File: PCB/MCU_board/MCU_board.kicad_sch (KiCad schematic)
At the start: 4 parts, among them IC3 ESP32-S3-WROOM-1-N4R8, J13 Conn_01x15, J14 Conn_01x15

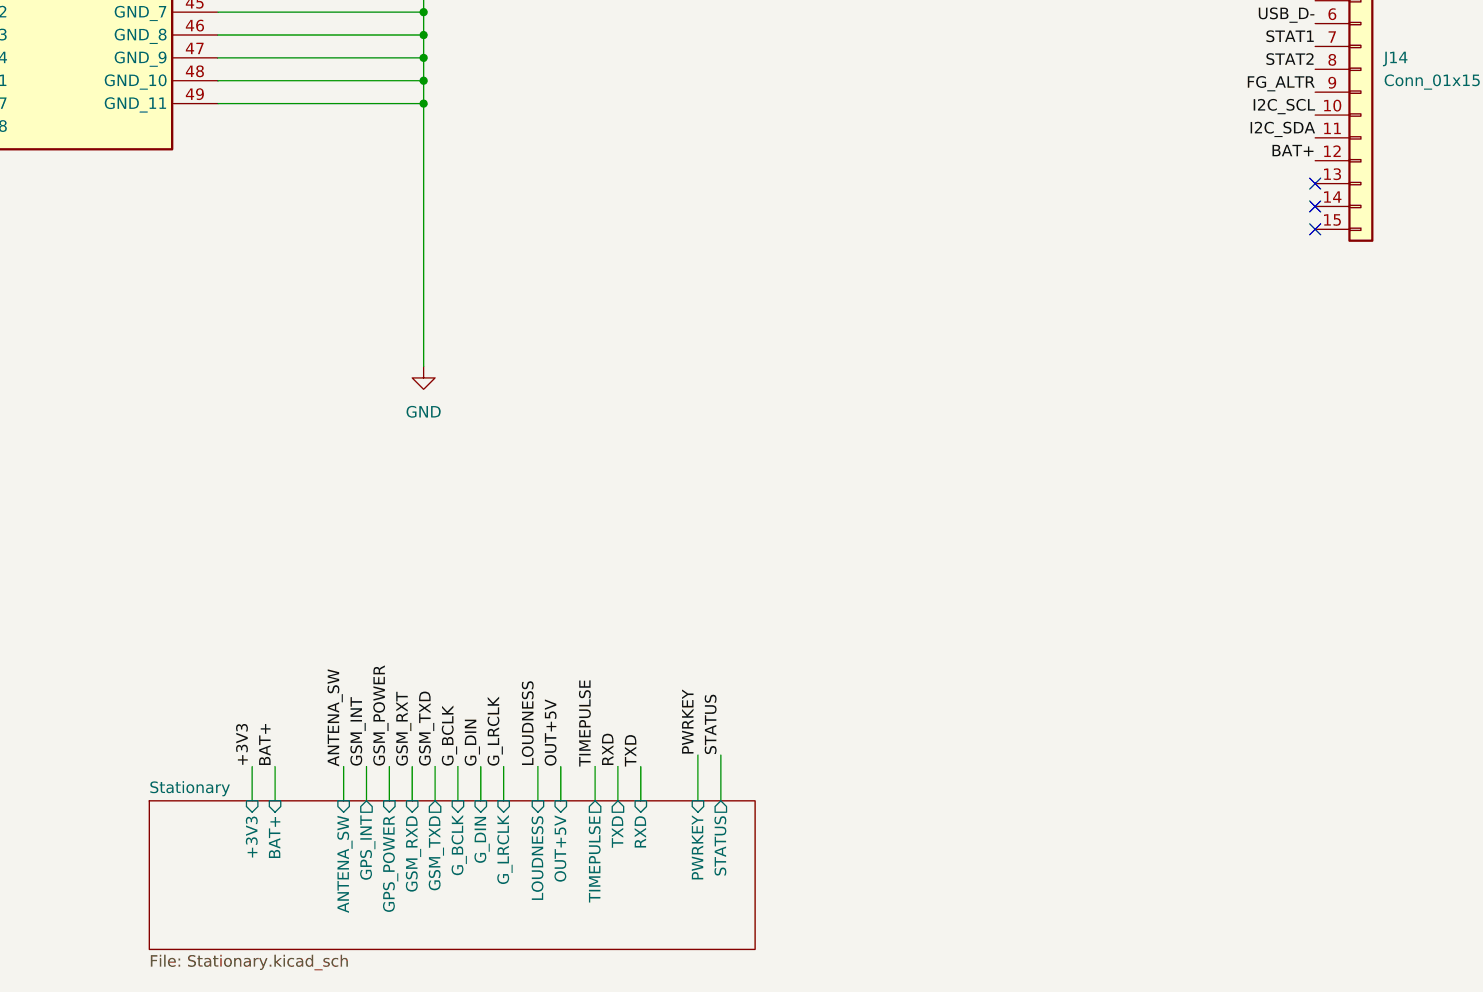
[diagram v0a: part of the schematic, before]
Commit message: routing and holes added
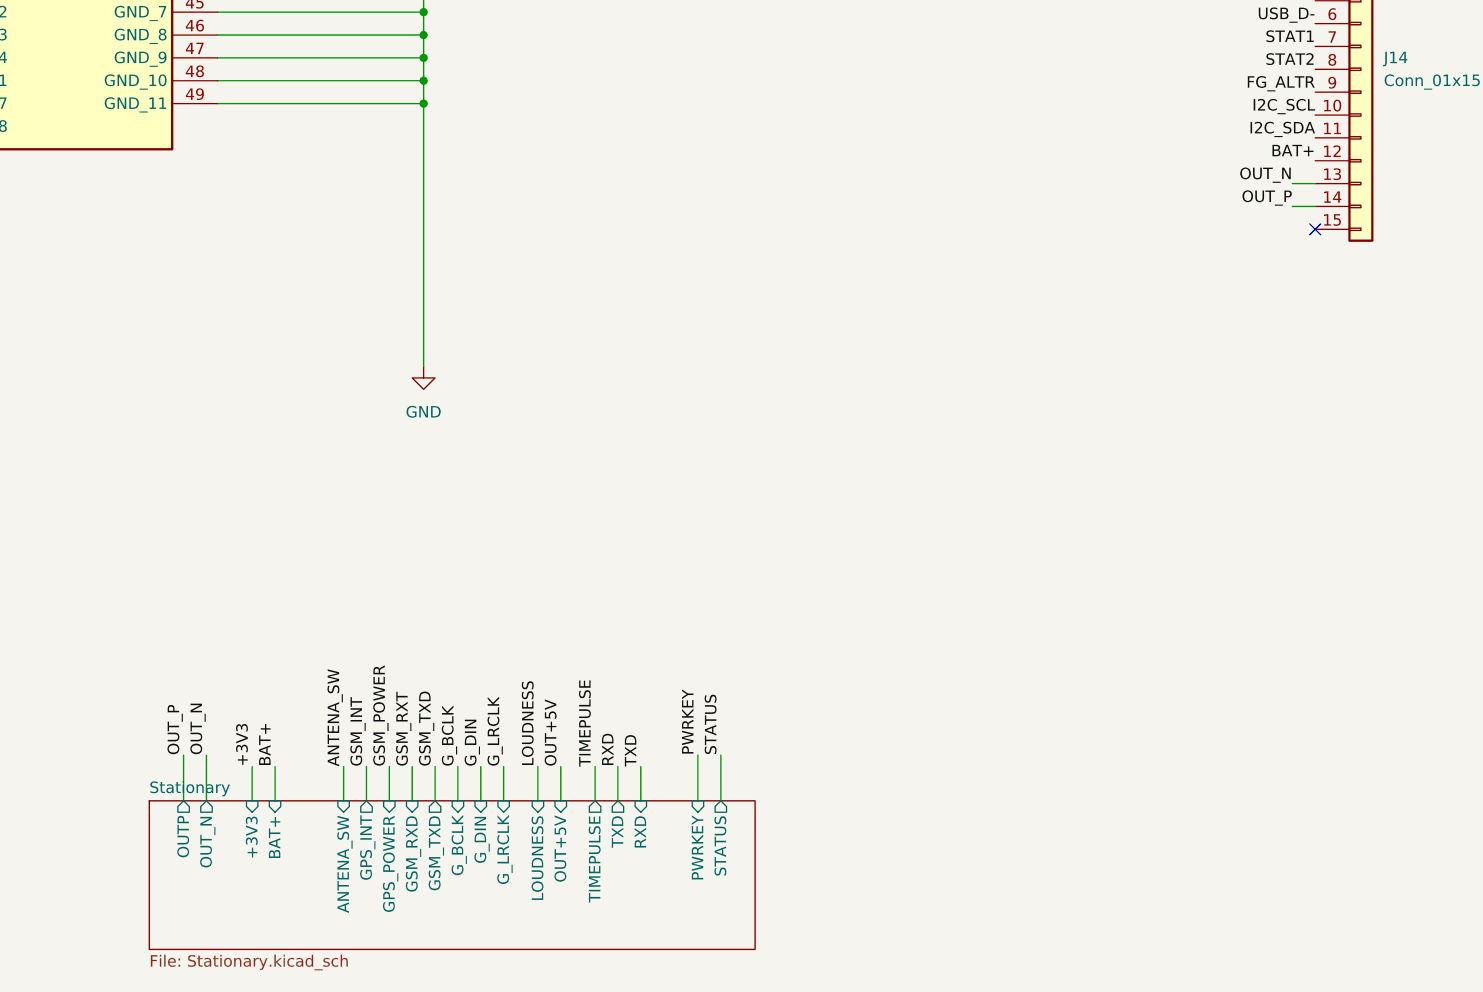
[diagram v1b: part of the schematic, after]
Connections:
- net OUT_N: now reaches J14.13 (Pin_13)
- net OUT_P: now reaches J14.14 (Pin_14)
- no-connect marks 8 -> 6
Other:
- sheet Stationary ports: added OUTP, OUT_N; removed none
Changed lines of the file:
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@@
-	)
-	(no_connect
-		(at 227.33 105.41)
 	)
 	(no_connect
@@
 	)
 	(no_connect
-		(at 227.33 102.87)
-	)
-	(no_connect
 		(at 237.49 31.75)
 	)
@@
 	(wire
 		(pts
+			(xy 104.14 166.37) (xy 104.14 171.45)
+		)
+		(stroke
+			(width 0)
+			(type default)
+		)
+	)
+	(wire
+		(pts
 			(xy 128.27 86.36) (xy 128.27 88.9)
 		)
@@
 	(wire
 		(pts
+			(xy 224.79 105.41) (xy 227.33 105.41)
+		)
+		(stroke
+			(width 0)
+			(type default)
+		)
+	)
+	(wire
+		(pts
 			(xy 59.69 40.64) (xy 72.39 40.64)
 		)
@@
 	(wire
 		(pts
+			(xy 101.6 166.37) (xy 101.6 171.45)
+		)
+		(stroke
+			(width 0)
+			(type default)
+		)
+	)
+	(wire
+		(pts
 			(xy 59.69 83.82) (xy 72.39 83.82)
 		)
@@
 		(pts
 			(xy 128.27 93.98) (xy 128.27 123.19)
+		)
+		(stroke
+			(width 0)
+			(type default)
+		)
+	)
+	(wire
+		(pts
+			(xy 224.79 102.87) (xy 227.33 102.87)
 		)
 		(stroke
@@
 		)
 	)
+	(label "OUT_N"
+		(at 104.14 166.37 90)
+		(effects
+			(font
+				(size 1.27 1.27)
+			)
+			(justify left bottom)
+		)
+	)
 	(label "TIMEPULSE"
 		(at 66.04 53.34 180)
@@
 		)
 	)
+	(label "OUT_N"
+		(at 224.79 102.87 180)
+		(effects
+			(font
+				(size 1.27 1.27)
+			)
+			(justify right bottom)
+		)
+	)
 	(label "G_BCLK"
 		(at 60.96 73.66 180)
@@
 		)
 	)
+	(label "OUT_P"
+		(at 224.79 105.41 180)
+		(effects
+			(font
+				(size 1.27 1.27)
+			)
+			(justify right bottom)
+		)
+	)
 	(label "GSM_POWER"
 		(at 124.46 167.64 90)
+		(effects
+			(font
+				(size 1.27 1.27)
+			)
+			(justify left bottom)
+		)
+	)
+	(label "OUT_P"
+		(at 101.6 166.37 90)
 		(effects
 			(font
@@
 			(effects
 				(font
+					(size 1.27 1.27)
+				)
+				(justify right)
+			)
+		)
+		(pin "OUTP" output
+			(at 101.6 171.45 90)
+			(effects
+				(font
+					(size 1.27 1.27)
+				)
+				(justify right)
+			)
+		)
+		(pin "OUT_N" output
+			(at 104.14 171.45 90)
+			(effects
+				(font

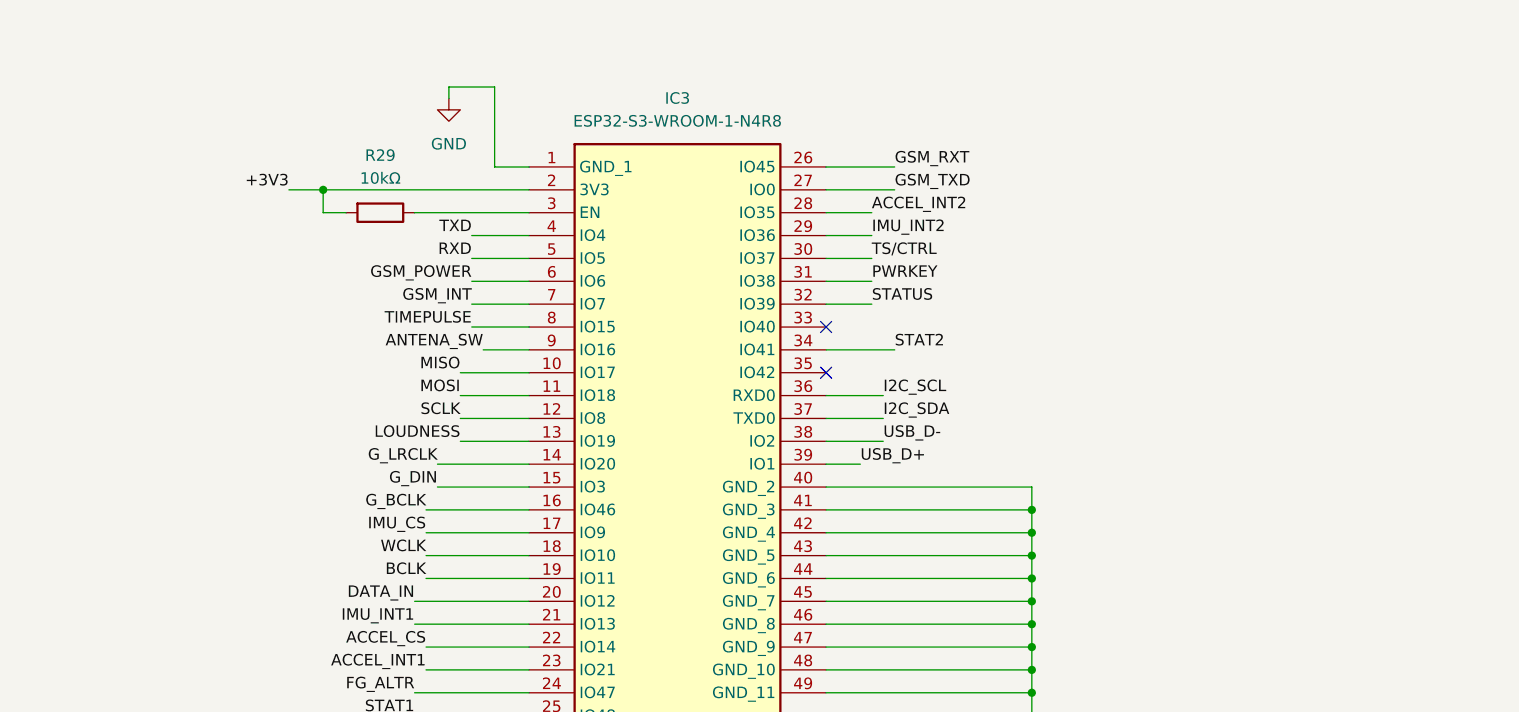
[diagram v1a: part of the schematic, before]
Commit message: programming MCU pins
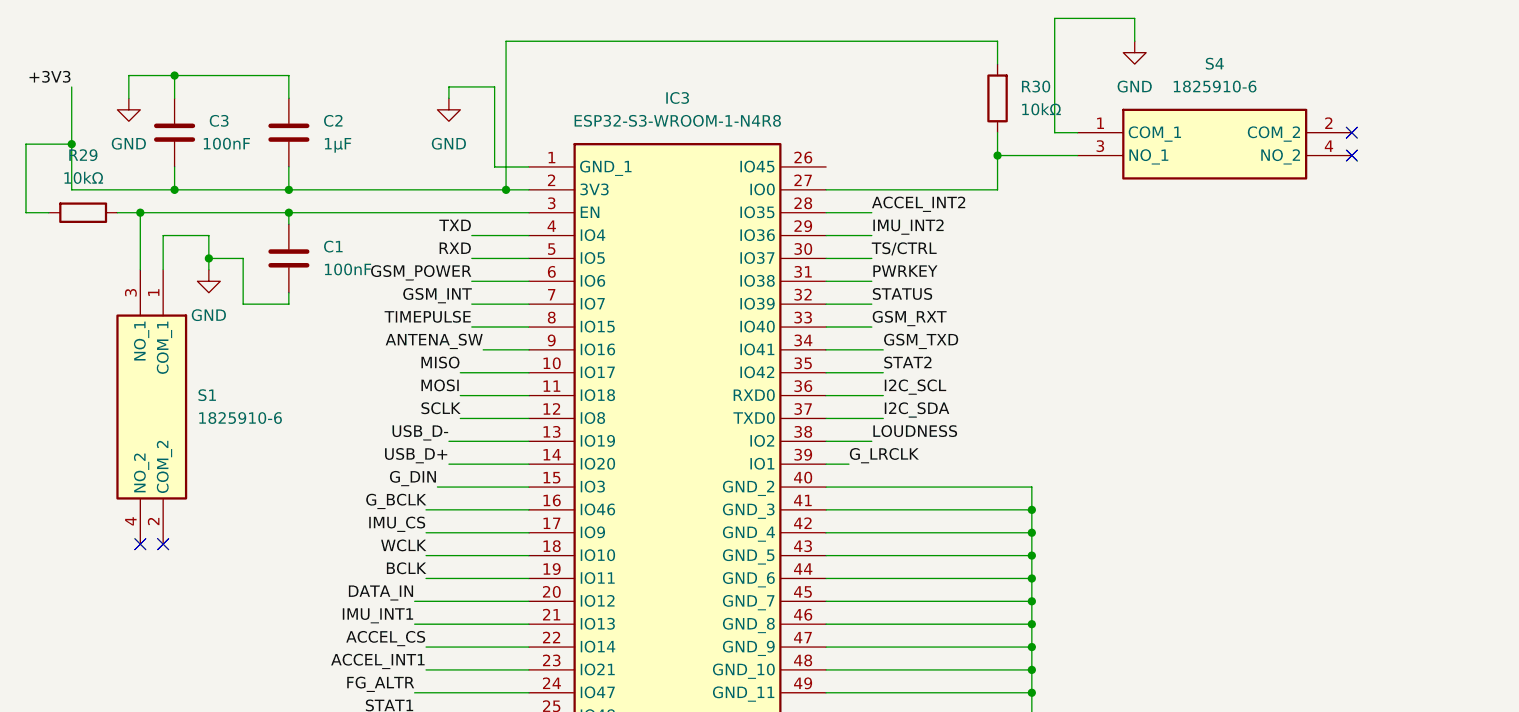
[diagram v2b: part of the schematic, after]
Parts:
- added C1, C3: 100nF, symbol Device:C
- added C2: 1μF, symbol Device:C
- added R30: 10kΩ, Resistor_THT:R_Axial_DIN0207_L6.3mm_D2.5mm_P7.62mm_Horizontal, symbol Device:R
- added S1, S4: 1825910-6, 18259106, symbol 1825910-6:1825910-6
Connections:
- net +3V3: now also C2.2, C3.2, R30.2
- net GND: now also C1.2, C2.1, C3.1, S1.1 (COM_1), S4.1 (COM_1)
- net GSM_RXT: now also IC3.33 (IO40); no longer IC3.26 (IO45)
- net GSM_TXD: now also IC3.34 (IO41); no longer IC3.27 (IO0)
- net G_LRCLK: now also IC3.39 (IO1); no longer IC3.14 (IO20)
- net LOUDNESS: now also IC3.38 (IO2); no longer IC3.13 (IO19)
- net STAT2: now also IC3.35 (IO42); no longer IC3.34 (IO41)
- net USB_D+: now also IC3.14 (IO20); no longer IC3.39 (IO1)
- net USB_D-: now also IC3.13 (IO19); no longer IC3.38 (IO2)
- net at IC3.3 (EN), R29.1: now also C1.1, S1.3 (NO_1)
- new net: IC3.27 (IO0), R30.1, S4.3 (NO_1)
- no-connect marks 6 -> 8

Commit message: everything before jlc template
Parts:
- removed J13, J14: Conn_01x15, Connector_PinHeader_2.54mm:PinHeader_1x15_P2.54mm_Vertical, symbol Connector_Generic:Conn_01x15
- added J1: DS1013-40SSIB1-B-0, DS1013-40SSIB1-B-0:DS101340SSIB1B0, symbol DS1013-40SSIB1-B-0:DS1013-40SSIB1-B-0
- C1, C2, C3: footprint (none) -> Capacitor_THT:C_Disc_D5.0mm_W2.5mm_P2.50mm
- S1, S4: footprint 18259106 -> 1825910-6:18259106
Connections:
- net +3V3: now also J1.1
- net ACCEL_CS: now also J1.24
- net ACCEL_INT1: now also J1.22
- net ACCEL_INT2: now also J1.20
- net BAT+: now also J1.23
- net BCLK: now also J1.18
- net DATA_IN: now also J1.16
- net FG_ALTR: now also J1.17
- net I2C_SCL: now also J1.19
- net I2C_SDA: now also J1.21
- net IMU_CS: now also J1.14
- net IMU_INT1: now also J1.12
- net IMU_INT2: now also J1.10
- net LOUDNESS: now also J1.7
- net MISO: now also J1.8
- net MOSI: now also J1.6
- net OUT+5V: now also J1.5
- net OUT_N: now also J1.25
- net OUT_P: now also J1.27
- net SCLK: now also J1.4
- net STAT1: now also J1.13
- net STAT2: now also J1.15
- net TS/CTRL: now also J1.3
- net USB_D+: now also J1.9
- net USB_D-: now also J1.11
- net WCLK: now also J1.2
- no-connect marks 8 -> 19

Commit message: verifying schematic and 3V8 power for gsm
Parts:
- removed C2: 1μF, Capacitor_THT:C_Disc_D5.0mm_W2.5mm_P2.50mm, symbol Device:C
- added C4: 1μF, symbol Device:C_Polarized
- C1: value 100nF -> 1μF
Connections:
- net +3V3: now also C4.2
- net GND: now also C4.1
- net 3V8: now reaches J1.26
- no-connect marks 19 -> 18
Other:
- sheet Stationary ports: added 3V8; removed none
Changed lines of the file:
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@@
 	)
 	(no_connect
-		(at 274.32 68.58)
-	)
-	(no_connect
 		(at 274.32 78.74)
 	)
@@
 	(wire
 		(pts
+			(xy 168.91 182.88) (xy 165.1 182.88)
+		)
+		(stroke
+			(width 0)
+			(type default)
+		)
+	)
+	(wire
+		(pts
 			(xy 132.08 167.64) (xy 132.08 171.45)
 		)
@@
 		)
 	)
+	(label "3V8"
+		(at 168.91 182.88 0)
+		(effects
+			(font
+				(size 1.27 1.27)
+			)
+			(justify left bottom)
+		)
+	)
 	(label "PWRKEY"
 		(at 110.49 48.26 0)
@@
 		)
 	)
+	(label "3V8"
+		(at 274.32 68.58 0)
+		(effects
+			(font
+				(size 1.27 1.27)
+			)
+			(justify left bottom)
+		)
+	)
 	(label "BAT+"
 		(at 251.46 66.04 180)
@@
 	)
 	(symbol
-		(lib_id "Device:C")
-		(at 45.72 31.75 0)
-		(unit 1)
-		(body_style 1)
-		(exclude_from_sim no)
-		(in_bom yes)
-		(on_board yes)
-		(in_pos_files yes)
-		(dnp no)
-		(fields_autoplaced yes)
-		(property "Reference" "C2"
-			(at 49.53 30.4799 0)
-			(show_name no)
-			(do_not_autoplace no)
-			(effects
-				(font
-					(size 1.27 1.27)
-				)
-				(justify left)
-			)
-		)
-		(property "Value" "1μF"
-			(at 49.53 33.0199 0)
-			(show_name no)
-			(do_not_autoplace no)
-			(effects
-				(font
-					(size 1.27 1.27)
-				)
-				(justify left)
-			)
-		)
-		(property "Footprint" "Capacitor_THT:C_Disc_D5.0mm_W2.5mm_P2.50mm"
-			(at 46.6852 35.56 0)
-			(hide yes)
-			(show_name no)
-			(do_not_autoplace no)
-			(effects
-				(font
-					(size 1.27 1.27)
-				)
-			)
-		)
-		(property "Datasheet" ""
-			(at 45.72 31.75 0)
-			(hide yes)
-			(show_name no)
-			(do_not_autoplace no)
-			(effects
-				(font
-					(size 1.27 1.27)
-				)
-			)
-		)
-		(property "Description" "Unpolarized capacitor"
-			(at 45.72 31.75 0)
-			(hide yes)
-			(show_name no)
-			(do_not_autoplace no)
-			(effects
-				(font
-					(size 1.27 1.27)
-				)
-			)
-		)
-		(pin "2"
-		)
-		(pin "1"
-		)
-		(instances
-			(project "MCU_board"
-				(path "/498aac81-136e-41bd-a3ff-29bc0732936d"
-					(reference "C2")
-					(unit 1)
-				)
-			)
-		)
-	)
-	(symbol
 		(lib_id "Device:R")
 		(at 22.86 40.64 270)
@@
 	)
 	(symbol
+		(lib_id "Device:C_Polarized")
+		(at 45.72 31.75 0)
+		(unit 1)
+		(body_style 1)
+		(exclude_from_sim no)
+		(in_bom yes)
+		(on_board yes)
+		(in_pos_files yes)
+		(dnp no)
+		(fields_autoplaced yes)
+		(property "Reference" "C4"
+			(at 49.53 29.5909 0)
+			(show_name no)
+			(do_not_autoplace no)
+			(effects
+				(font
+					(size 1.27 1.27)
+				)
+				(justify left)
+			)
+		)
+		(property "Value" "1μF"
+			(at 49.53 32.1309 0)
+			(show_name no)
+			(do_not_autoplace no)
+			(effects
+				(font
+					(size 1.27 1.27)
+				)
+				(justify left)
+			)
+		)
+		(property "Footprint" ""
+			(at 46.6852 35.56 0)
+			(hide yes)
+			(show_name no)
+			(do_not_autoplace no)
+			(effects
+				(font
+					(size 1.27 1.27)
+				)
+			)
+		)
+		(property "Datasheet" ""
+			(at 45.72 31.75 0)
+			(hide yes)
+			(show_name no)
+			(do_not_autoplace no)
+			(effects
+				(font
+					(size 1.27 1.27)
+				)
+			)
+		)
+		(property "Description" "Polarized capacitor"
+			(at 45.72 31.75 0)
+			(hide yes)
+			(show_name no)
+			(do_not_autoplace no)
+			(effects
+				(font
+					(size 1.27 1.27)
+				)
+			)
+		)
+		(pin "1"
+		)
+		(pin "2"
+		)
+		(instances
+			(project "MCU_board"
+				(path "/498aac81-136e-41bd-a3ff-29bc0732936d"
+					(reference "C4")
+					(unit 1)
+				)
+			)
+		)
+	)
+	(symbol
 		(lib_id "DS1013-40SSIB1-B-0:DS1013-40SSIB1-B-0")
 		(at 251.46 38.1 0)
@@
 			)
 		)
-		(property "Value" "100nF"
+		(property "Value" "1μF"
 			(at 49.53 46.9899 0)
 			(show_name no)
@@
 			(effects
 				(font
+					(size 1.27 1.27)
+				)
+				(justify right)
+			)
+		)
+		(pin "3V8" output
+			(at 165.1 182.88 0)
+			(effects
+				(font

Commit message: ECR passed
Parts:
- C4: footprint (none) -> Capacitor_THT:CP_Radial_Tantal_D5.0mm_P2.50mm
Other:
- sheet Stationary ports: added none; removed BAT+
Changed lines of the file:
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@@
-	(wire
-		(pts
-			(xy 45.72 50.8) (xy 40.64 50.8)
-		)
-		(stroke
-			(width 0)
-			(type default)
-		)
-	)
 	(wire
 		(pts
@@
 	(wire
 		(pts
-			(xy 111.76 167.64) (xy 111.76 171.45)
-		)
-		(stroke
-			(width 0)
-			(type default)
-		)
-	)
-	(wire
-		(pts
 			(xy 60.96 76.2) (xy 72.39 76.2)
 		)
@@
 		(pts
 			(xy 133.35 34.29) (xy 124.46 34.29)
+		)
+		(stroke
+			(width 0)
+			(type default)
+		)
+	)
+	(wire
+		(pts
+			(xy 40.64 50.8) (xy 45.72 50.8)
 		)
 		(stroke
@@
 	(label "MISO"
 		(at 274.32 45.72 0)
-		(effects
-			(font
-				(size 1.27 1.27)
-			)
-			(justify left bottom)
-		)
-	)
-	(label "BAT+"
-		(at 111.76 167.64 90)
 		(effects
 			(font
@@
 			)
 		)
-		(property "Footprint" ""
+		(property "Footprint" "Capacitor_THT:CP_Radial_Tantal_D5.0mm_P2.50mm"
 			(at 46.6852 35.56 0)
 			(hide yes)
@@
 			(effects
 				(font
-					(size 1.27 1.27)
-				)
-				(justify right)
-			)
-		)
-		(pin "BAT+" input
-			(at 111.76 171.45 90)
-			(effects
-				(font
